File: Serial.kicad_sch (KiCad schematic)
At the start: 4 parts, among them J3 D09P33E4GX00LF

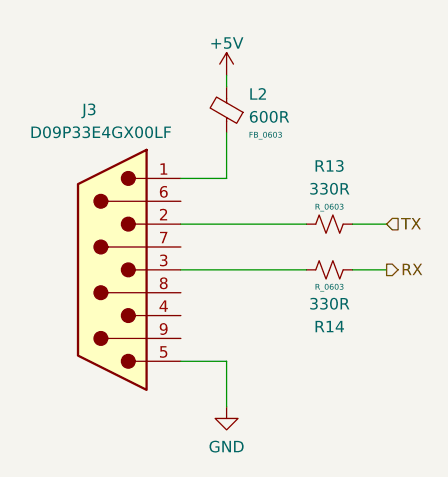
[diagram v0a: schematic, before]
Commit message: Rebuild using new output scripts
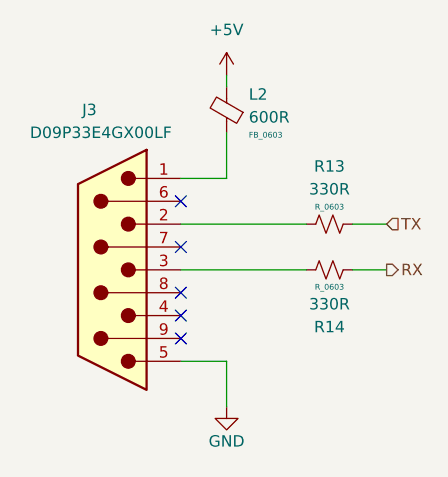
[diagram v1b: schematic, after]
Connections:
- no-connect marks 0 -> 5
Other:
- company: (none) -> TL Embedded Ltd
- title: (none) -> Serial-Ethernet
